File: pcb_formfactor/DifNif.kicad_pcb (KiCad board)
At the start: 2 copper layers, 98.8 x 93 mm, 83 parts, among them J1 DBA-ESDI, J2 PROG, J3 SDCARD_DM3AT-SF-PEJM5, J4 HPLA_PORT, U1 ICE40HX4K-TQ144, U10 74LVC4245, U11 74LCX07, U12 74VHCT125, U13 Teensy4_1, U14 74LVC4245, U2 SST26VF080A-104I/SN, U3 APX803S00-29SA-7, U4 AP2114HA-3.3, U5 AP2114HA-1.2, U6 74LVC4245, U7 74LVC4245, U8 74LVC4245, U9 74LVC4245, X1 ASE-xxxMHz

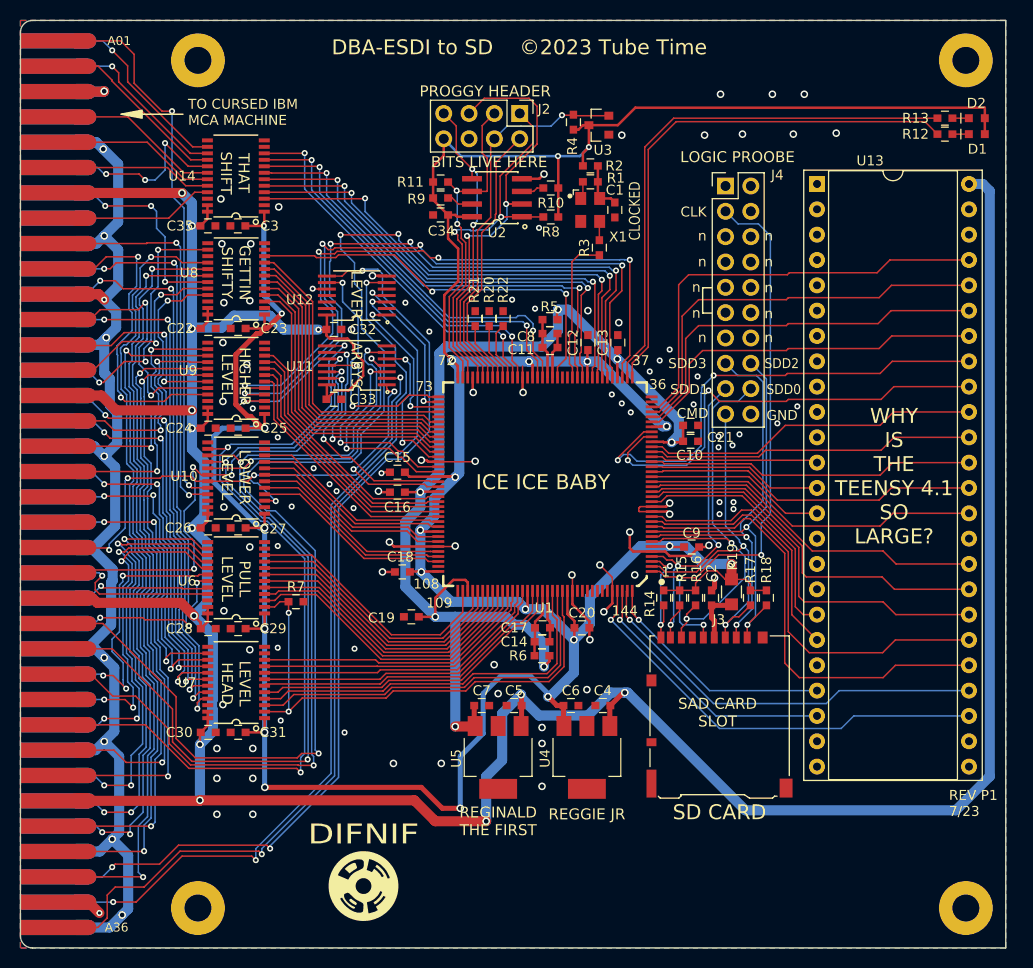
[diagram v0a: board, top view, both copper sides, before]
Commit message: Add diode OR, add clock series R
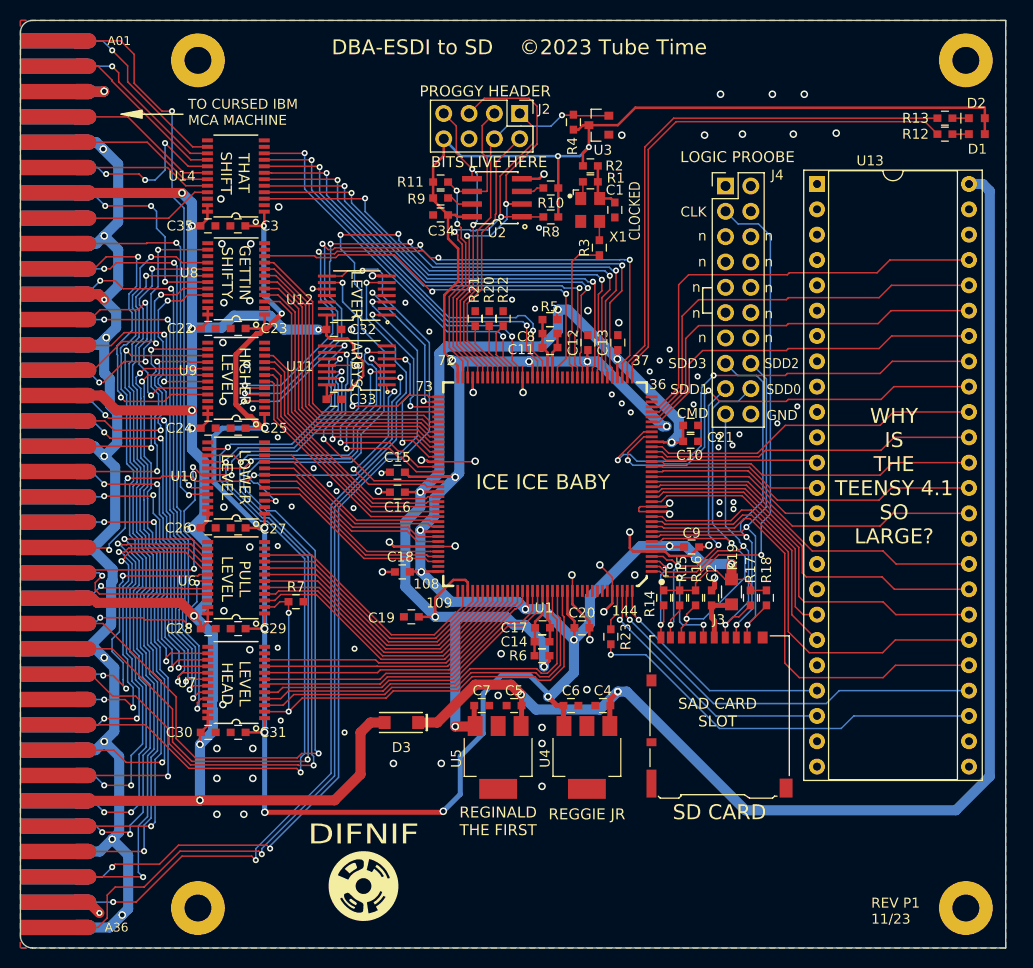
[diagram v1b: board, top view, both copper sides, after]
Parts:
- added D3: PMEG10010ELR, Active:SOD3716X117, F.Cu at (129.4, 108.4)
- added R23: 10, Passive:RESC1608X55, F.Cu at (150.4, 99.8)
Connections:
- C4 pad 1: +5V -> +5VD
- C5 pad 1: +5V -> +5VD
- U1 pad 141: /TN35 -> Net-(U1-Pad141)
- U13 pad 48: +5V -> +5VD
- U4 pad 1: +5V -> +5VD
- U5 pad 1: +5V -> +5VD
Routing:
- net +5V: track 338.8 -> 195.6 mm, vias 13 -> 10
- net +5VD: track 0.00 -> 135.1 mm, vias 0 -> 2
- net Net-(U1-Pad141): track 0.00 -> 4.12 mm
- net /TN35: track 44.1 -> 40.6 mm
- net +3V3: track 369.8 -> 370.8 mm
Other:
- board text added: "REV P1 11/23"
- board text removed: "REV P1 7/23"

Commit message: fabout form factor pcb
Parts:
- moved C2 23.7 mm to (170.6, 117.3), turned to -90 degrees
- moved J3 21.5 mm to (181.0, 116.0), turned to 90 degrees
- moved D1 9.69 mm to (180.2, 42.6)
- moved D2 9.69 mm to (180.2, 41.0)
- moved R12 9.69 mm to (177.0, 42.6)
- moved R13 9.69 mm to (177.0, 41.0)
- moved U13 6.90 mm to (171.1, 47.5)
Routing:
- net /SDCard/SD_SWITCH: track 11.6 -> 43.5 mm
- net /SD_D1: track 34.6 -> 63.6 mm
- net /SD_CLK: track 58.3 -> 87.0 mm
- net /SD_D0: track 42.6 -> 68.2 mm
- net Net-(C2-Pad1): track 5.38 -> 27.4 mm
- net /SD_D3: track 41.8 -> 63.3 mm
- net /SD_CMD: track 38.1 -> 57.8 mm
- net /SD_D2: track 42.1 -> 61.5 mm
- net /TN37: track 45.8 -> 38.6 mm
- net +5VD: track 135.1 -> 142.0 mm
- net /TN27: track 26.4 -> 19.7 mm
- net /TN38: track 43.2 -> 36.6 mm
- net /TN26: track 25.2 -> 18.9 mm
- net /TN39: track 40.0 -> 34.2 mm
- net +3V3: track 370.8 -> 365.7 mm
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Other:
- board text added: "DBA-ESDI to SD"
- board text added: "WRONG LEVEL KRONK"
- board text added: "©2023 Tube Time"
- board text removed: "DBA-ESDI to SD ©2023 Tube Time"
- board text removed: "LEVEL HEAD"
